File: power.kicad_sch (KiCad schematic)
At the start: 18 parts, among them U1 TPS61201DRC, U4 BQ25176J

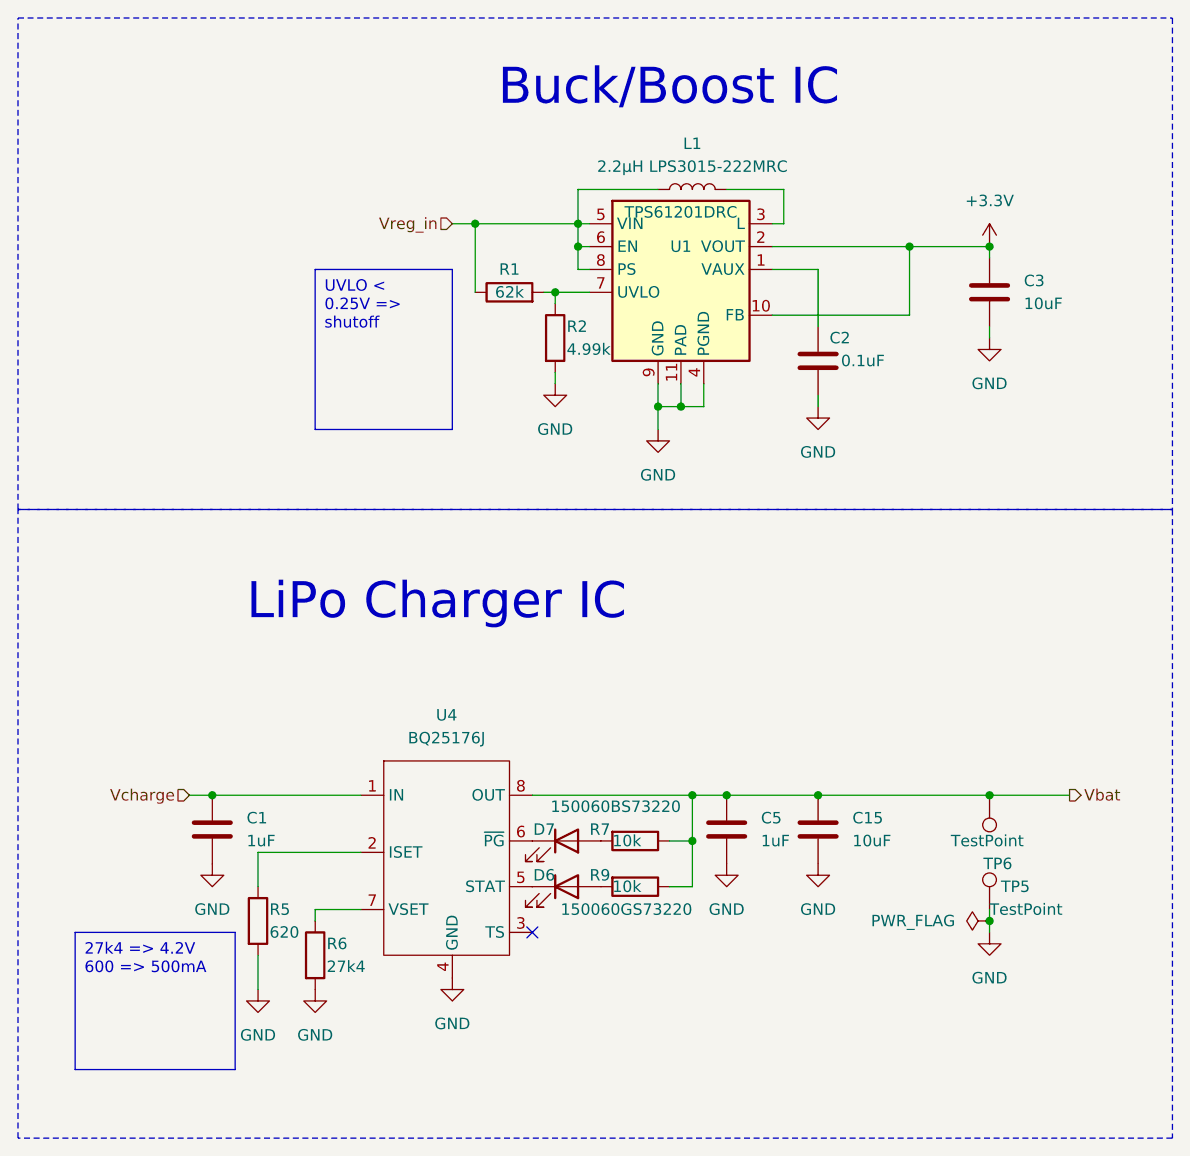
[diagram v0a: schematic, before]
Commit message: Implement Simon's layout suggestions
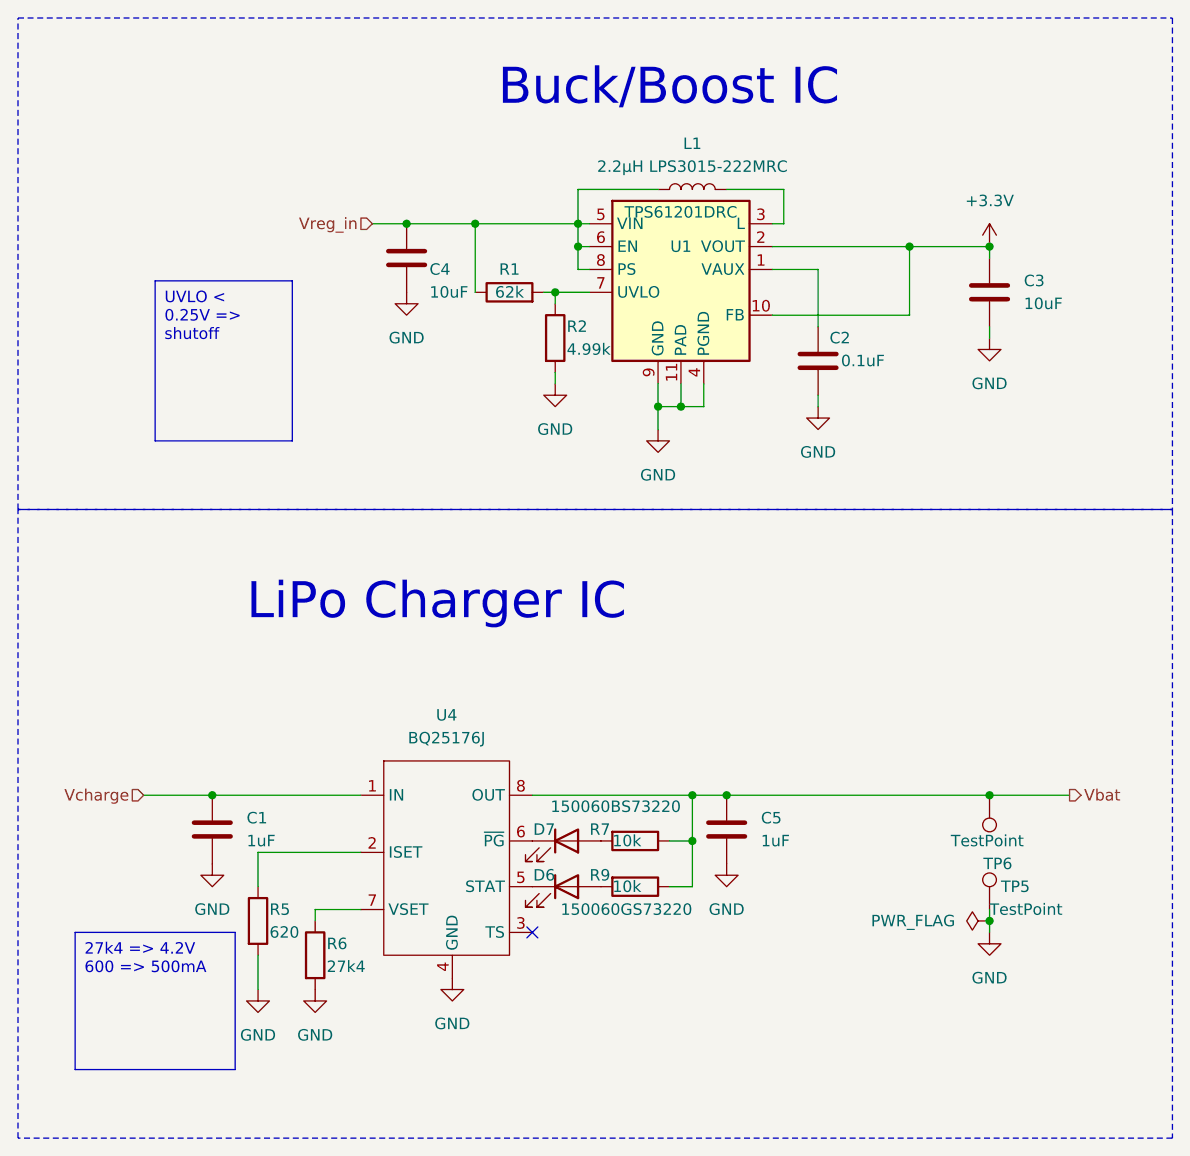
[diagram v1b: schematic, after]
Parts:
- removed C15: 10uF, Capacitor_SMD:C_0805_2012Metric, symbol Device:C
- added C4: 10uF, Capacitor_SMD:C_0805_2012Metric, symbol Device:C
- U1: footprint Package_SON:Texas_S-PVSON-N10_ThermalVias -> bier:Texas_S-PVSON-N10_ThermalVias
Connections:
- net GND: now also C4.2
- net Vreg_in: now also C4.1
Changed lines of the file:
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@@
   (junction (at 68.58 57.15) (diameter 0) (color 0 0 0 0)
   )
+  (junction (at 60.96 57.15) (diameter 0) (color 0 0 0 0)
+  )
   (junction (at 125.73 59.69) (diameter 0) (color 0 0 0 0)
   )
   (junction (at 92.71 125.73) (diameter 0) (color 0 0 0 0)
-  )
-  (junction (at 106.68 120.65) (diameter 0) (color 0 0 0 0)
   )
   (junction (at 116.84 59.69) (diameter 0) (color 0 0 0 0)
@@
     (stroke (width 0) (type default))
   )
-  (wire (pts (xy 96.52 120.65) (xy 106.68 120.65))
+  (wire (pts (xy 96.52 120.65) (xy 125.73 120.65))
     (stroke (width 0) (type default))
   )
@@
     (stroke (width 0) (type default))
   )
-  (wire (pts (xy 66.04 57.15) (xy 68.58 57.15))
+  (wire (pts (xy 57.15 57.15) (xy 60.96 57.15))
     (stroke (width 0) (type default))
   )
@@
     (stroke (width 0) (type default))
   )
-  (wire (pts (xy 106.68 120.65) (xy 125.73 120.65))
-    (stroke (width 0) (type default))
-  )
   (wire (pts (xy 125.73 69.85) (xy 125.73 68.58))
     (stroke (width 0) (type default))
@@
     (stroke (width 0) (type default))
   )
+  (wire (pts (xy 60.96 57.15) (xy 68.58 57.15))
+    (stroke (width 0) (type default))
+  )
   (wire (pts (xy 116.84 59.69) (xy 125.73 59.69))
     (stroke (width 0) (type default))
@@
     (stroke (width 0) (type default))
   )
-  (wire (pts (xy 36.83 120.65) (xy 39.37 120.65))
+  (wire (pts (xy 31.75 120.65) (xy 39.37 120.65))
     (stroke (width 0) (type default))
   )
@@
   )
   (text_box "UVLO < 0.25V => shutoff"
-    (at 50.8 62.23 0) (size 15.24 17.78)
+    (at 33.02 63.5 0) (size 15.24 17.78)
     (stroke (width 0) (type default))
     (fill (type none))
@@
     (effects (font (size 4 4)) (justify left bottom))
   )
-  (hierarchical_label "Vcharge" (shape input) (at 36.83 120.65 180) (fields_autoplaced)
+  (hierarchical_label "Vcharge" (shape input) (at 31.75 120.65 180) (fields_autoplaced)
     (effects (font (size 1.27 1.27)) (justify right))
   )
@@
     (effects (font (size 1.27 1.27)) (justify left))
   )
-  (hierarchical_label "Vreg_in" (shape input) (at 66.04 57.15 180) (fields_autoplaced)
+  (hierarchical_label "Vreg_in" (shape input) (at 57.15 57.15 180) (fields_autoplaced)
     (effects (font (size 1.27 1.27)) (justify right))
   )
@@
       (effects (font (size 1.27 1.27)))
     )
-    (property "Footprint" "Package_SON:Texas_S-PVSON-N10_ThermalVias" (at 91.44 73.66 0)
+    (property "Footprint" "bier:Texas_S-PVSON-N10_ThermalVias" (at 91.44 73.66 0)
       (effects (font (size 1.27 1.27)) hide)
     )
@@
       (effects (font (size 1.27 1.27)) hide)
     )
-    (property "Datasheet" "https://www.digikey.at/en/products/detail/w%C3%BCrth-elektronik/150060BS73220/8557159?s=N4IgTCBcDaIIwFYAMSBsSBCBlA7AZjDCRAF0BfIA" (at 78.74 125.73 0)
+    (property "Datasheet" "~" (at 78.74 125.73 0)
       (effects (font (size 1.27 1.27)) hide)
     )
@@
         (path "/a4ffe097-37ef-4e19-a91a-ae57f4a5aad1/06d9cd17-cb19-4cdd-8e67-c41d1b4a676e"
           (reference "D7") (unit 1)
+        )
+      )
+    )
+  )
+  (symbol (lib_id "power:GND") (at 60.96 64.77 0) (unit 1)
+    (in_bom yes) (on_board yes) (dnp no) (fields_autoplaced)
+    (property "Reference" "#PWR044" (at 60.96 71.12 0)
+      (effects (font (size 1.27 1.27)) hide)
+    )
+    (property "Value" "GND" (at 60.96 69.85 0)
+      (effects (font (size 1.27 1.27)))
+    )
+    (property "Footprint" "" (at 60.96 64.77 0)
+      (effects (font (size 1.27 1.27)) hide)
+    )
+    (property "Datasheet" "" (at 60.96 64.77 0)
+      (effects (font (size 1.27 1.27)) hide)
+    )
+    (pin "1")
+    (instances
+      (project "bierdeckel"
+        (path "/a4ffe097-37ef-4e19-a91a-ae57f4a5aad1/06d9cd17-cb19-4cdd-8e67-c41d1b4a676e"
+          (reference "#PWR044") (unit 1)
         )
       )
@@
       (effects (font (size 1.27 1.27)) hide)
     )
-    (property "Datasheet" "https://www.digikey.at/en/products/detail/w%C3%BCrth-elektronik/150060GS73220/8557160?s=N4IgTCBcDaIIwFYAMSBsSDiBlA7AZjDCRAF0BfIA" (at 78.74 130.81 0)
+    (property "Datasheet" "~" (at 78.74 130.81 0)
       (effects (font (size 1.27 1.27)) hide)
     )
@@
     )
   )
-  (symbol (lib_id "power:GND") (at 106.68 128.27 0) (unit 1)
-    (in_bom yes) (on_board yes) (dnp no) (fields_autoplaced)
-    (property "Reference" "#PWR044" (at 106.68 134.62 0)
-      (effects (font (size 1.27 1.27)) hide)
-    )
-    (property "Value" "GND" (at 106.68 133.35 0)
-      (effects (font (size 1.27 1.27)))
-    )
-    (property "Footprint" "" (at 106.68 128.27 0)
-      (effects (font (size 1.27 1.27)) hide)
-    )
-    (property "Datasheet" "" (at 106.68 128.27 0)
-      (effects (font (size 1.27 1.27)) hide)
-    )
-    (pin "1")
-    (instances
-      (project "bierdeckel"
-        (path "/a4ffe097-37ef-4e19-a91a-ae57f4a5aad1/06d9cd17-cb19-4cdd-8e67-c41d1b4a676e"
-          (reference "#PWR044") (unit 1)
-        )
-      )
-    )
-  )
   (symbol (lib_id "Device:R") (at 44.45 134.62 0) (unit 1)
     (in_bom yes) (on_board yes) (dnp no)
@@
         (path "/a4ffe097-37ef-4e19-a91a-ae57f4a5aad1/06d9cd17-cb19-4cdd-8e67-c41d1b4a676e"
           (reference "R5") (unit 1)
-        )
-      )
-    )
-  )
-  (symbol (lib_id "Device:C") (at 106.68 124.46 0) (unit 1)
-    (in_bom yes) (on_board yes) (dnp no) (fields_autoplaced)
-    (property "Reference" "C15" (at 110.49 123.19 0)
-      (effects (font (size 1.27 1.27)) (justify left))
-    )
-    (property "Value" "10uF" (at 110.49 125.73 0)
-      (effects (font (size 1.27 1.27)) (justify left))
-    )
-    (property "Footprint" "Capacitor_SMD:C_0805_2012Metric" (at 107.6452 128.27 0)
-      (effects (font (size 1.27 1.27)) hide)
-    )
-    (property "Datasheet" "~" (at 106.68 124.46 0)
-      (effects (font (size 1.27 1.27)) hide)
-    )
-    (property "mpn" "CL21A106KPFNNNF" (at 106.68 124.46 0)
-      (effects (font (size 1.27 1.27)) hide)
-    )
-    (pin "1")
-    (pin "2")
-    (instances
-      (project "bierdeckel"
-        (path "/a4ffe097-37ef-4e19-a91a-ae57f4a5aad1/06d9cd17-cb19-4cdd-8e67-c41d1b4a676e"
-          (reference "C15") (unit 1)
         )
       )
@@
         )
       )
+    )
+  )
+  (symbol (lib_id "Device:C") (at 60.96 60.96 0) (unit 1)
+    (in_bom yes) (on_board yes) (dnp no)
+    (property "Reference" "C4" (at 63.5 62.23 0)
+      (effects (font (size 1.27 1.27)) (justify left))
+    )
+    (property "Value" "10uF" (at 63.5 64.77 0)
+      (effects (font (size 1.27 1.27)) (justify left))
+    )
+    (property "Footprint" "Capacitor_SMD:C_0805_2012Metric" (at 61.9252 64.77 0)
+      (effects (font (size 1.27 1.27)) hide)
+    )
+    (property "Datasheet" "~" (at 60.96 60.96 0)
+      (effects (font (size 1.27 1.27)) hide)
+    )
+    (property "mpn" "CL21A106KPFNNNF" (at 60.96 60.96 0)
+      (effects (font (size 1.27 1.27)) hide)
+    )
+    (pin "1")
+    (pin "2")
+    (instances
+      (project "bierdeckel"
+        (path "/a4ffe097-37ef-4e19-a91a-ae57f4a5aad1/06d9cd17-cb19-4cdd-8e67-c41d1b4a676e"
+          (reference "C4") (unit 1)
+        )
+      )

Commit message: remove ATTiny; fix LED footprints; start cleanup
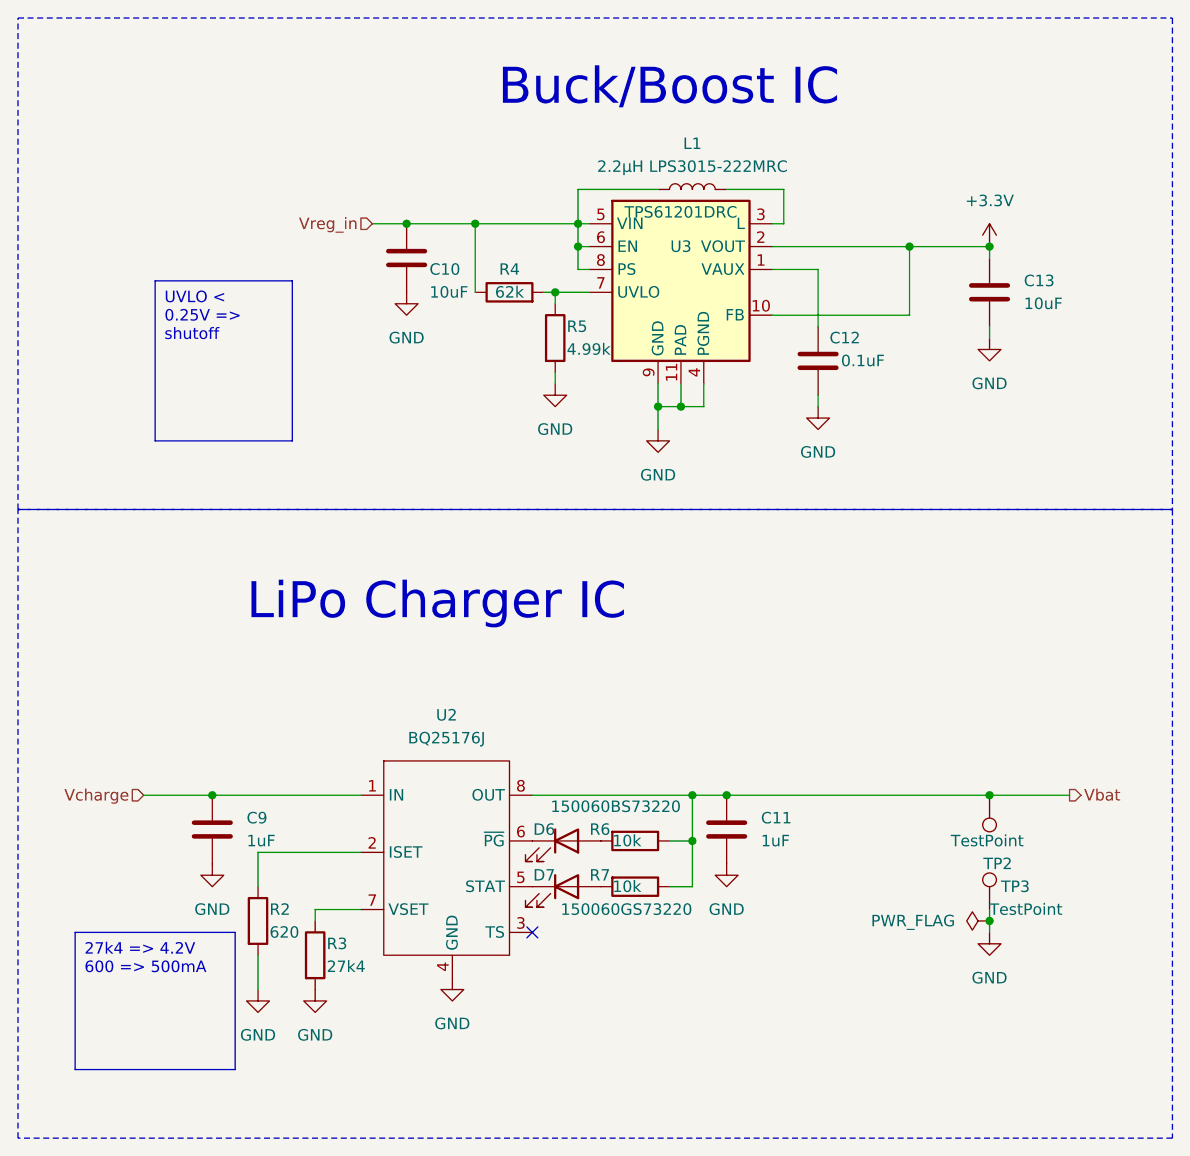
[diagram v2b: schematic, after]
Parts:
- renumbered C4 to C10, C5 to C11, C2 to C12, C3 to C13, C1 to C9, D7 to D6, D6 to D7, R5 to R2, R6 to R3, R1 to R4, R2 to R5, R7 to R6, R9 to R7, TP6 to TP2, TP5 to TP3, U4 to U2, U1 to U3

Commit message: improve layout further
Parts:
- U3: footprint bier:Texas_S-PVSON-N10_ThermalVias -> Package_SON:Texas_S-PVSON-N10_ThermalVias
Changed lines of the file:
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@@
 			)
 		)
-		(property "Footprint" "bier:Texas_S-PVSON-N10_ThermalVias"
+		(property "Footprint" "Package_SON:Texas_S-PVSON-N10_ThermalVias"
 			(at 91.44 73.66 0)
 			(effects
@@
 			)
 		)
-		(property "Description" ""
+		(property "Description" "Low Input Voltage Synchronous Boost Converter With 1.3A Switches, Fixed 5V Output Voltage, 0.3-5.5V Input Voltage, VSON-10"
 			(at 91.44 62.23 0)
 			(effects
@@
 			)
 		)
-		(property "Description" ""
+		(property "Description" "Power symbol creates a global label with name \"GND\" , ground"
 			(at 39.37 128.27 0)
 			(effects
@@
 			)
 		)
-		(property "Description" ""
+		(property "Description" "Unpolarized capacitor"
 			(at 39.37 124.46 0)
 			(effects
@@
 			)
 		)
-		(property "Description" ""
+		(property "Description" "Unpolarized capacitor"
 			(at 96.52 124.46 0)
 			(effects
@@
 			)
 		)
-		(property "Description" ""
+		(property "Description" "Power symbol creates a global label with name \"GND\" , ground"
 			(at 44.45 142.24 0)
 			(effects
@@
 			)
 		)
-		(property "Description" ""
+		(property "Description" "Light emitting diode"
 			(at 78.74 125.73 0)
 			(effects
@@
 			)
 		)
-		(property "Description" ""
+		(property "Description" "Power symbol creates a global label with name \"GND\" , ground"
 			(at 60.96 64.77 0)
 			(effects
@@
 			)
 		)
-		(property "Description" ""
+		(property "Description" "Resistor"
 			(at 72.39 64.77 0)
 			(effects
@@
 			)
 		)
-		(property "Description" ""
+		(property "Description" "Power symbol creates a global label with name \"GND\" , ground"
 			(at 96.52 128.27 0)
 			(effects
@@
 			)
 		)
-		(property "Description" ""
+		(property "Description" "Special symbol for telling ERC where power comes from"
 			(at 125.73 134.62 0)
 			(effects
@@
 			)
 		)
-		(property "Description" ""
+		(property "Description" "Unpolarized capacitor"
 			(at 106.68 72.39 0)
 			(effects
@@
 			)
 		)
-		(property "Description" ""
+		(property "Description" "Power symbol creates a global label with name \"GND\" , ground"
 			(at 88.9 80.01 0)
 			(effects
@@
 			)
 		)
-		(property "Description" ""
+		(property "Description" "Resistor"
 			(at 86.36 130.81 0)
 			(effects
@@
 			)
 		)
-		(property "Description" ""
+		(property "Description" "Unpolarized capacitor"
 			(at 125.73 64.77 0)
 			(effects
@@
 			)
 		)
-		(property "Description" ""
+		(property "Description" "Light emitting diode"
 			(at 78.74 130.81 0)
 			(effects
@@
 			)
 		)
-		(property "Description" ""
+		(property "Description" "test point"
 			(at 125.73 133.35 0)
 			(effects
@@
 			)
 		)
-		(property "Description" ""
+		(property "Description" "Power symbol creates a global label with name \"GND\" , ground"
 			(at 125.73 69.85 0)
 			(effects
@@
 			)
 		)
-		(property "Description" ""
+		(property "Description" "Resistor"
 			(at 44.45 134.62 0)
 			(effects
@@
 			)
 		)
-		(property "Description" ""
+		(property "Description" "Power symbol creates a global label with name \"GND\" , ground"
 			(at 77.47 74.93 0)
 			(effects
@@
 			)
 		)
-		(property "Description" ""
+		(property "Description" "test point"
 			(at 125.73 120.65 0)
 			(effects
@@
 			)
 		)
-		(property "Description" ""
+		(property "Description" "Power symbol creates a global label with name \"+3.3V\""
 			(at 125.73 59.69 0)
 			(effects
@@
 			)
 		)
-		(property "Description" ""
+		(property "Description" "Power symbol creates a global label with name \"GND\" , ground"
 			(at 66.04 140.97 0)
 			(effects
@@
 			)
 		)
-		(property "Description" ""
+		(property "Description" "Power symbol creates a global label with name \"GND\" , ground"
 			(at 50.8 142.24 0)
 			(effects
@@
 			)
 		)
-		(property "Description" ""
+		(property "Description" "Resistor"
 			(at 86.36 125.73 0)
 			(effects
@@
 			)
 		)
-		(property "Description" ""
+		(property "Description" "Inductor"
 			(at 92.71 53.34 0)
 			(effects
@@
 			)
 		)
-		(property "Description" ""
+		(property "Description" "Power symbol creates a global label with name \"GND\" , ground"
 			(at 106.68 77.47 0)
 			(effects
@@
 			)
 		)
-		(property "Description" ""
+		(property "Description" "Power symbol creates a global label with name \"GND\" , ground"
 			(at 125.73 135.89 0)
 			(effects
@@
 			)
 		)
-		(property "Description" ""
+		(property "Description" "Resistor"
 			(at 50.8 138.43 0)
 			(effects
@@
 			)
 		)
-		(property "Description" ""
+		(property "Description" "Resistor"
 			(at 77.47 69.85 0)
 			(effects
@@
 			)
 		)
-		(property "Description" ""
+		(property "Description" "Unpolarized capacitor"
 			(at 60.96 60.96 0)
 			(effects
